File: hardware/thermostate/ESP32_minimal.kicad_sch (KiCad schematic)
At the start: 28 parts, among them IC1 L8050QLT1G, IC2 L8050QLT1G, P1 USB_C_Plug_USB2.0, SW1 SW_Push, SW2 SW_Push, U1 ESP32-S3-WROOM-1, U2 LM1117-3.3

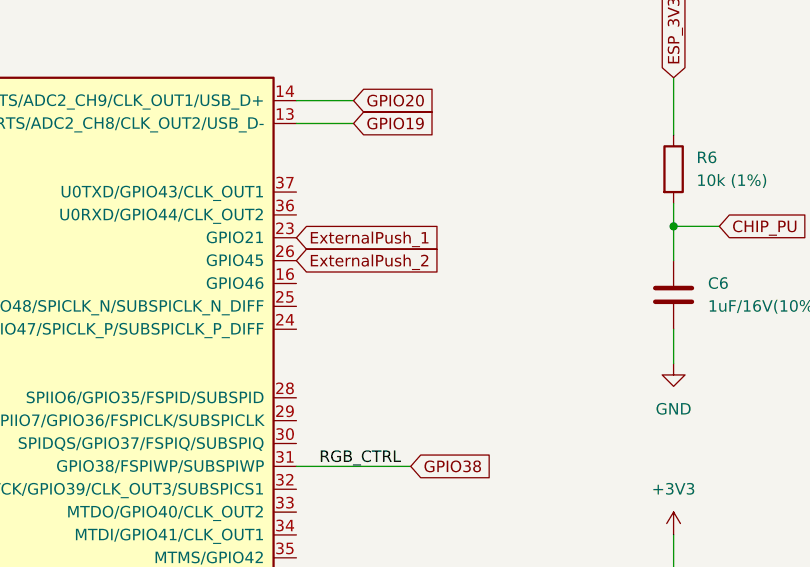
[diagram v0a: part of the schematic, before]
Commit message: Add temperature sensor
Signed-off-by: Javier <javierfernandezvillasante@gmail.com>
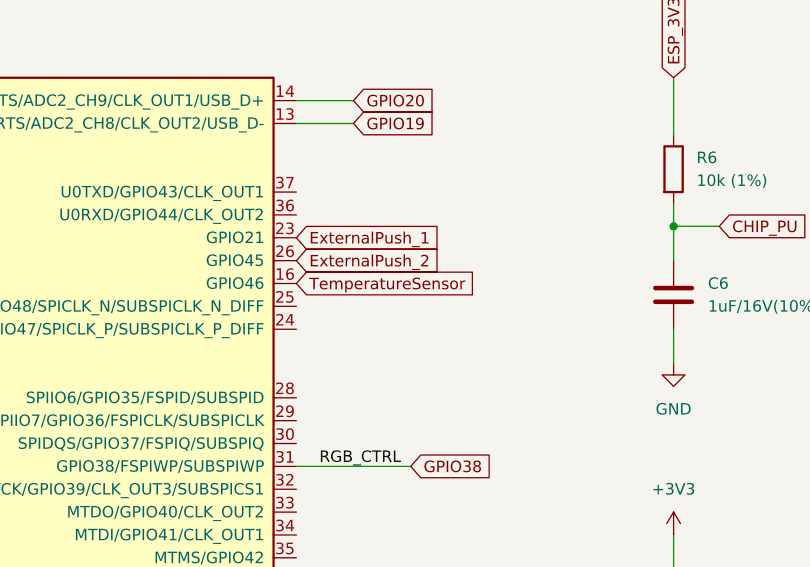
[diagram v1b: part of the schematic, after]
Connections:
- net TemperatureSensor: now reaches U1.16 (GPIO46)
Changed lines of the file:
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@@
+    )
+  )
+  (global_label "TemperatureSensor" (shape input) (at 214.63 53.34 0) (fields_autoplaced)
+    (effects (font (size 1.27 1.27)) (justify left))
+    (property "Intersheet References" "${INTERSHEET_REFS}" (id 0) (at 235.1255 53.2606 0)
+      (effects (font (size 1.27 1.27)) (justify left) hide)
     )
   )

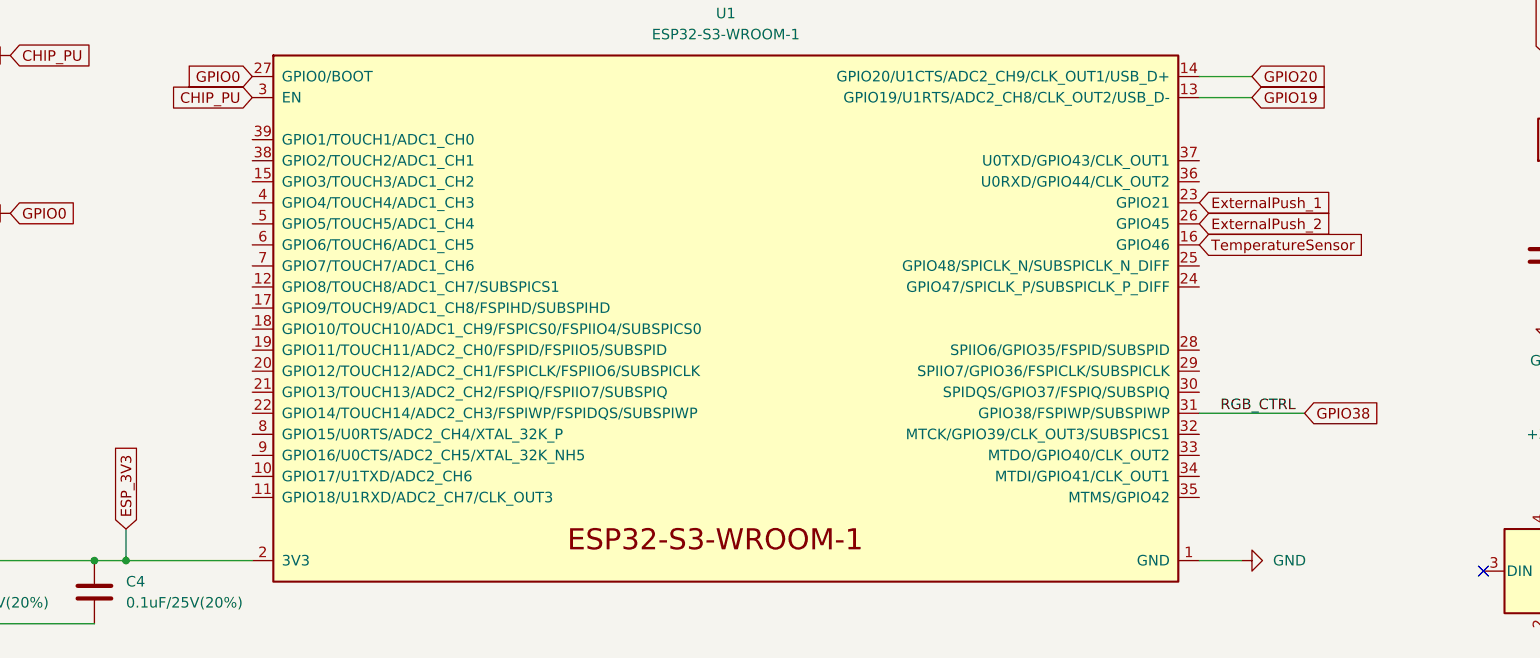
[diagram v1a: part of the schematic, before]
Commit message: Add Components PCB
Signed-off-by: Javier <javierfernandezvillasante@gmail.com>
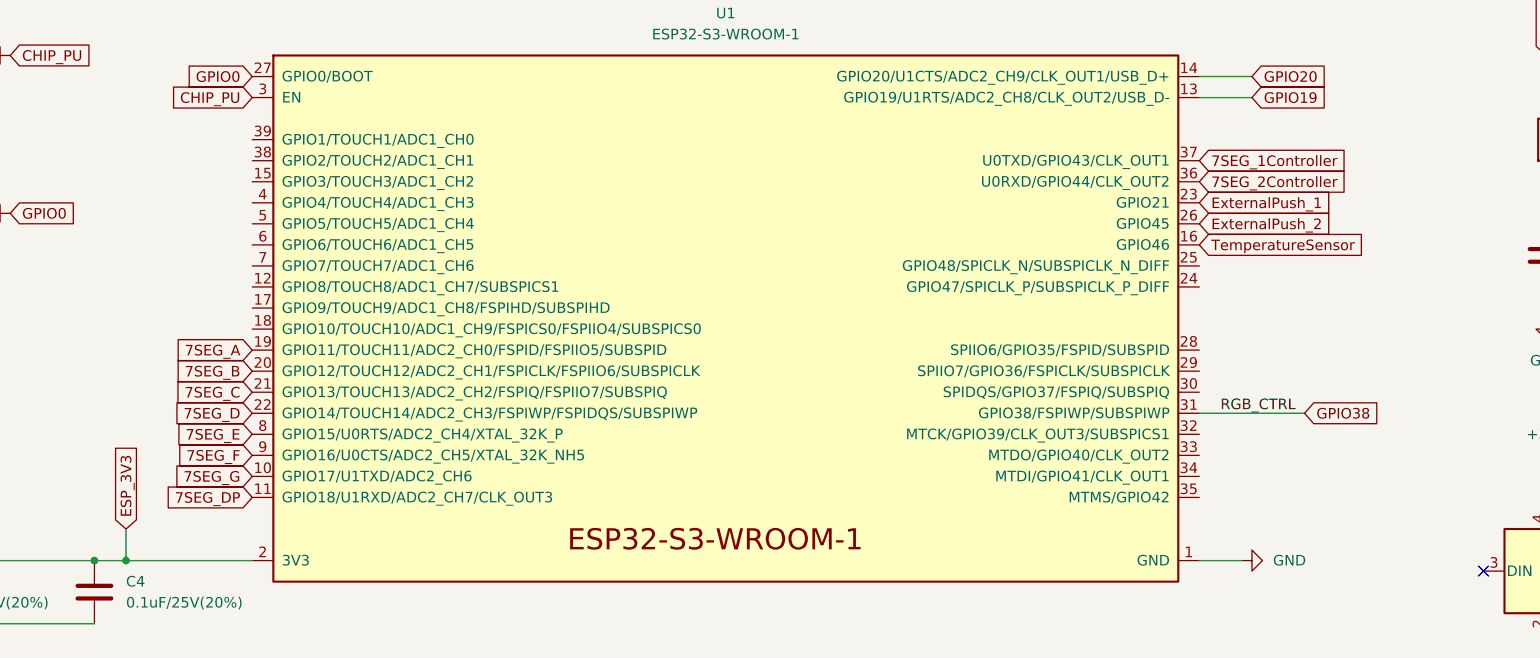
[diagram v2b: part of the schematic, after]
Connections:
- net 7SEG_G: now reaches U1.10 (GPIO17/U1TXD/ADC2_CH6)
- net 7SEG_DP: now reaches U1.11 (GPIO18/U1RXD/ADC2_CH7/CLK_OUT3)
- net 7SEG_A: now reaches U1.19 (GPIO11/TOUCH11/ADC2_CH0/FSPID/FSPIIO5/SUBSPID)
- net 7SEG_B: now reaches U1.20 (GPIO12/TOUCH12/ADC2_CH1/FSPICLK/FSPIIO6/SUBSPICLK)
- net 7SEG_C: now reaches U1.21 (GPIO13/TOUCH13/ADC2_CH2/FSPIQ/FSPIIO7/SUBSPIQ)
- net 7SEG_D: now reaches U1.22 (GPIO14/TOUCH14/ADC2_CH3/FSPIWP/FSPIDQS/SUBSPIWP)
- net 7SEG_2Controller: now reaches U1.36 (U0RXD/GPIO44/CLK_OUT2)
- net 7SEG_1Controller: now reaches U1.37 (U0TXD/GPIO43/CLK_OUT1)
- net 7SEG_E: now reaches U1.8 (GPIO15/U0RTS/ADC2_CH4/XTAL_32K_P)
- net 7SEG_F: now reaches U1.9 (GPIO16/U0CTS/ADC2_CH5/XTAL_32K_NH5)
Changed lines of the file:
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@@
+    )
+  )
+  (global_label "7SEG_C" (shape input) (at 100.33 71.12 180) (fields_autoplaced)
+    (effects (font (size 1.27 1.27)) (justify right))
+    (property "Intersheet References" "${INTERSHEET_REFS}" (id 0) (at 90.8412 71.0406 0)
+      (effects (font (size 1.27 1.27)) (justify right) hide)
+    )
+  )
+  (global_label "7SEG_2Controller" (shape input) (at 214.63 45.72 0) (fields_autoplaced)
+    (effects (font (size 1.27 1.27)) (justify left))
+    (property "Intersheet References" "${INTERSHEET_REFS}" (id 0) (at 233.4926 45.7994 0)
+      (effects (font (size 1.27 1.27)) (justify left) hide)
+    )
+  )
+  (global_label "7SEG_D" (shape input) (at 100.33 73.66 180) (fields_autoplaced)
+    (effects (font (size 1.27 1.27)) (justify right))
+    (property "Intersheet References" "${INTERSHEET_REFS}" (id 0) (at 90.8412 73.5806 0)
+      (effects (font (size 1.27 1.27)) (justify right) hide)
     )
   )
@@
     (property "Intersheet References" "${INTERSHEET_REFS}" (id 0) (at 256.4606 19.9631 90)
       (effects (font (size 1.27 1.27)) (justify left) hide)
+    )
+  )
+  (global_label "7SEG_DP" (shape input) (at 100.33 83.82 180) (fields_autoplaced)
+    (effects (font (size 1.27 1.27)) (justify right))
+    (property "Intersheet References" "${INTERSHEET_REFS}" (id 0) (at 89.5712 83.7406 0)
+      (effects (font (size 1.27 1.27)) (justify right) hide)
     )
   )
@@
     )
   )
+  (global_label "7SEG_F" (shape input) (at 100.33 78.74 180) (fields_autoplaced)
+    (effects (font (size 1.27 1.27)) (justify right))
+    (property "Intersheet References" "${INTERSHEET_REFS}" (id 0) (at 91.0226 78.6606 0)
+      (effects (font (size 1.27 1.27)) (justify right) hide)
+    )
+  )
   (global_label "GPIO19" (shape input) (at 135.89 157.48 0) (fields_autoplaced)
     (effects (font (size 1.27 1.27)) (justify left))
@@
     (property "Intersheet References" "${INTERSHEET_REFS}" (id 0) (at 85.0106 77.1131 90)
       (effects (font (size 1.27 1.27)) (justify left) hide)
+    )
+  )
+  (global_label "7SEG_A" (shape input) (at 100.33 66.04 180) (fields_autoplaced)
+    (effects (font (size 1.27 1.27)) (justify right))
+    (property "Intersheet References" "${INTERSHEET_REFS}" (id 0) (at 91.0226 65.9606 0)
+      (effects (font (size 1.27 1.27)) (justify right) hide)
+    )
+  )
+  (global_label "7SEG_1Controller" (shape input) (at 214.63 43.18 0) (fields_autoplaced)
+    (effects (font (size 1.27 1.27)) (justify left))
+    (property "Intersheet References" "${INTERSHEET_REFS}" (id 0) (at 233.4926 43.2594 0)
+      (effects (font (size 1.27 1.27)) (justify left) hide)
+    )
+  )
+  (global_label "7SEG_E" (shape input) (at 100.33 76.2 180) (fields_autoplaced)
+    (effects (font (size 1.27 1.27)) (justify right))
+    (property "Intersheet References" "${INTERSHEET_REFS}" (id 0) (at 90.9621 76.1206 0)
+      (effects (font (size 1.27 1.27)) (justify right) hide)
     )
   )
@@
     )
   )
+  (global_label "7SEG_B" (shape input) (at 100.33 68.58 180) (fields_autoplaced)
+    (effects (font (size 1.27 1.27)) (justify right))
+    (property "Intersheet References" "${INTERSHEET_REFS}" (id 0) (at 90.8412 68.5006 0)
+      (effects (font (size 1.27 1.27)) (justify right) hide)
+    )
+  )
   (global_label "CHIP_PU" (shape input) (at 261.62 46.99 0) (fields_autoplaced)
     (effects (font (size 1.27 1.27)) (justify left))
@@
       (effects (font (size 1.27 1.27)) (justify right) hide)
     )
+  )
+  (global_label "7SEG_G" (shape input) (at 100.33 81.28 180) (fields_autoplaced)
+    (effects (font (size 1.27 1.27)) (justify right))
+    (property "Intersheet References" "${INTERSHEET_REFS}" (id 0) (at 90.8412 81.2006 0)
+      (effects (font (size 1.27 1.27)) (justify right) hide)
+    )

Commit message: Start desing PCB
Signed-off-by: Javier <javierfernandezvillasante@gmail.com>
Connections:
- net GPIO19 renamed USB_N
- net GPIO20 renamed USB_P
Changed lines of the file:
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@@
+    (stroke (width 0) (type default) (color 0 0 0 0))
+  )
+  (wire (pts (xy 214.63 33.02) (xy 226.06 33.02))
     (stroke (width 0) (type default) (color 0 0 0 0))
   )
@@
     (stroke (width 0) (type default) (color 0 0 0 0))
   )
-  (wire (pts (xy 220.98 33.02) (xy 214.63 33.02))
-    (stroke (width 0) (type default) (color 0 0 0 0))
-  )
   (wire (pts (xy 21.59 39.37) (xy 21.59 30.48))
     (stroke (width 0) (type default) (color 0 0 0 0))
@@
     (stroke (width 0) (type default) (color 0 0 0 0))
   )
-  (wire (pts (xy 220.98 35.56) (xy 214.63 35.56))
+  (wire (pts (xy 214.63 35.56) (xy 226.06 35.56))
     (stroke (width 0) (type default) (color 0 0 0 0))
   )
@@
     (effects (font (size 3 3) bold italic) (justify left bottom))
   )
+  (label "USB_P" (at 49.53 162.56 0)
+    (effects (font (size 1.27 1.27)) (justify left bottom))
+  )
   (label "RGB_CTRL" (at 217.17 73.66 0)
     (effects (font (size 1.27 1.27)) (justify left bottom))
   )
+  (label "USB_N" (at 226.06 35.56 0)
+    (effects (font (size 1.27 1.27)) (justify left bottom))
+  )
+  (label "USB_N" (at 49.53 157.48 0)
+    (effects (font (size 1.27 1.27)) (justify left bottom))
+  )
+  (label "USB_P" (at 135.89 162.56 0)
+    (effects (font (size 1.27 1.27)) (justify left bottom))
+  )
+  (label "USB_P" (at 226.06 33.02 0)
+    (effects (font (size 1.27 1.27)) (justify left bottom))
+  )
+  (label "USB_N" (at 135.89 157.48 0)
+    (effects (font (size 1.27 1.27)) (justify left bottom))
+  )
   (global_label "GPIO0" (shape input) (at 41.91 62.23 0) (fields_autoplaced)
     (effects (font (size 1.27 1.27)) (justify left))
@@
     )
   )
-  (global_label "GPIO19" (shape input) (at 135.89 157.48 0) (fields_autoplaced)
-    (effects (font (size 1.27 1.27)) (justify left))
-    (property "Intersheet References" "${INTERSHEET_REFS}" (id 0) (at 145.1974 157.4006 0)
-      (effects (font (size 1.27 1.27)) (justify left) hide)
-    )
-  )
   (global_label "ESP_3V3" (shape input) (at 85.09 87.63 90) (fields_autoplaced)
     (effects (font (size 1.27 1.27)) (justify left))
@@
       (effects (font (size 1.27 1.27)) (justify left) hide)
     )
-  )
-  (global_label "GPIO20" (shape input) (at 135.89 162.56 0) (fields_autoplaced)
-    (effects (font (size 1.27 1.27)) (justify left))
-    (property "Intersheet References" "${INTERSHEET_REFS}" (id 0) (at 145.1974 162.4806 0)
-      (effects (font (size 1.27 1.27)) (justify left) hide)
-    )
-  )
-  (global_label "GPIO20" (shape input) (at 220.98 33.02 0) (fields_autoplaced)
-    (effects (font (size 1.27 1.27)) (justify left))
-    (property "Intersheet References" "${INTERSHEET_REFS}" (id 0) (at 230.2874 32.9406 0)
-      (effects (font (size 1.27 1.27)) (justify left) hide)
-    )
-  )
-  (global_label "GPIO19" (shape input) (at 220.98 35.56 0) (fields_autoplaced)
-    (effects (font (size 1.27 1.27)) (justify left))
-    (property "Intersheet References" "${INTERSHEET_REFS}" (id 0) (at 230.2874 35.4806 0)
-      (effects (font (size 1.27 1.27)) (justify left) hide)
-    )
